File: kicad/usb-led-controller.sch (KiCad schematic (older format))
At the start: 2 parts

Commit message: Adding initial schematic
The PWM outputs are driven with the microcontroller PWM. The WS2812
outputs are driven from UARTS with DMA capability.
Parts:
- removed J?: Conn_02x05_Odd_Even, symbol Connector_Generic:Conn_02x05_Odd_Even
- added C1: 4u7, Capacitor_SMD:C_0805_2012Metric, symbol Device:C
- added C2, C4, C8: 1u, Capacitor_SMD:C_0402_1005Metric, symbol Device:C
- added C3: 10u, Capacitor_SMD:C_0805_2012Metric, symbol Device:C
- added C5, C6, C7: 0u1, Capacitor_SMD:C_0402_1005Metric, symbol Device:C
- added J1: SWD, usb-led-controller:JST-SH-4, symbol Connector_Generic:Conn_01x04
- added J2: PWR, usb-led-controller:M20-88904, symbol Connector_Generic:Conn_01x04
- added J3: USB, usb-led-controller:M20-88904, symbol Connector_Generic:Conn_01x04
- added J4: PWM_0, usb-led-controller:M20-88904, symbol Connector_Generic:Conn_01x04
- added J5: PWM_1, usb-led-controller:M20-88904, symbol Connector_Generic:Conn_01x04
- added J6: WS2812_0, usb-led-controller:M20-88903, symbol Connector_Generic:Conn_01x03
- added J7: WS2812_1, usb-led-controller:M20-88903, symbol Connector_Generic:Conn_01x03
- added Q1, Q2, Q3, Q4, Q5, Q6: NVS4409N, Package_TO_SOT_SMD:SOT-323_SC-70, symbol Device:Q_NMOS_GSD
- added R1, R3, R5: 0, Resistor_SMD:R_0402_1005Metric, symbol Device:R
- added R2: 1K, Resistor_SMD:R_0402_1005Metric, symbol Device:R
- added R4: SPR, Resistor_SMD:R_0402_1005Metric, symbol Device:R
- added R6, R7, R8, R9: 33, Resistor_SMD:R_0402_1005Metric, symbol Device:R
- added U1, U2: SN74LV1T04, Package_TO_SOT_SMD:SOT-353_SC-70-5, symbol usb-led-controller:SN74LV1T04
- added U4: MIC5501-XYM5, Package_TO_SOT_SMD:SOT-23-5, symbol usb-led-controller:MIC5501-XYM5
- added U5: USBLC6, Package_TO_SOT_SMD:SOT-666, symbol usb-led-controller:USBLC6
- gave numbers to parts that had none: 1
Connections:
- net labels added: +12V, +3.3V, BOOT0, GATE_0_B, GATE_0_G, GATE_0_R, GATE_1_B, GATE_1_G, GATE_1_R, NRST, PWM_0_B, PWM_0_G, PWM_0_R, PWM_1_B, PWM_1_G, PWM_1_R, SWCLK, SWDIO, USB_D+, USB_D-, USB_D_R+, USB_D_R-, USB_D_TVS+, USB_D_TVS-, WS2812_0_DATA, WS2812_0_DATA_IO, WS2812_0_DATA_R, WS2812_1_DATA, WS2812_1_DATA_IO, WS2812_1_DATA_R
- wire segments 6 -> 164
- no-connect marks 5 -> 16
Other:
- note added: "PA0: TIM2_CH1\nPA1: TIM2_CH2\nPA2: TIM2_CH3\nPA3: TIM2_CH4\nPA6: TIM22_CH1\nPA7: TIM22_CH2\nPA9: USART1_TX\nPA14: USART2_TX (yep...hopefully no bricking)"
- moved on the sheet: U3

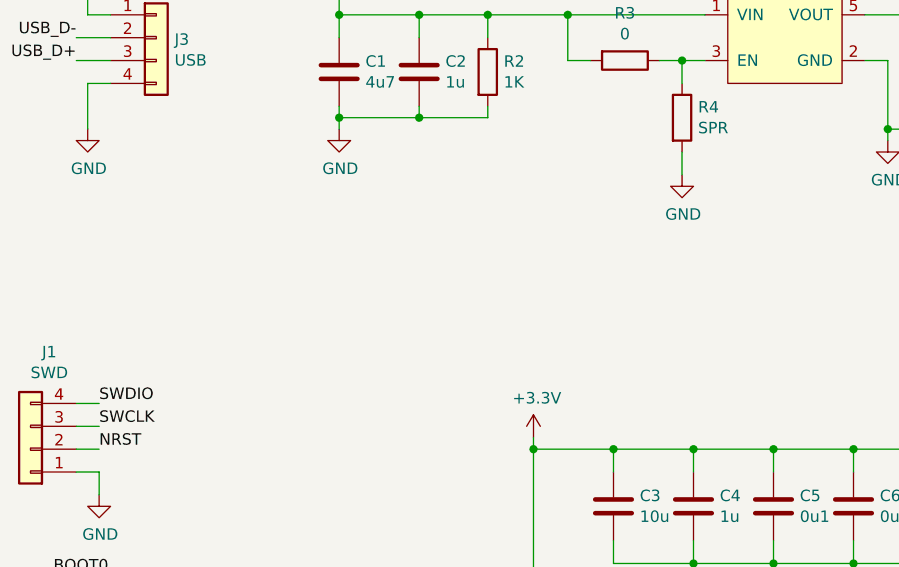
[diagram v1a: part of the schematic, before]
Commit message: Determined board form factor and placed connectors
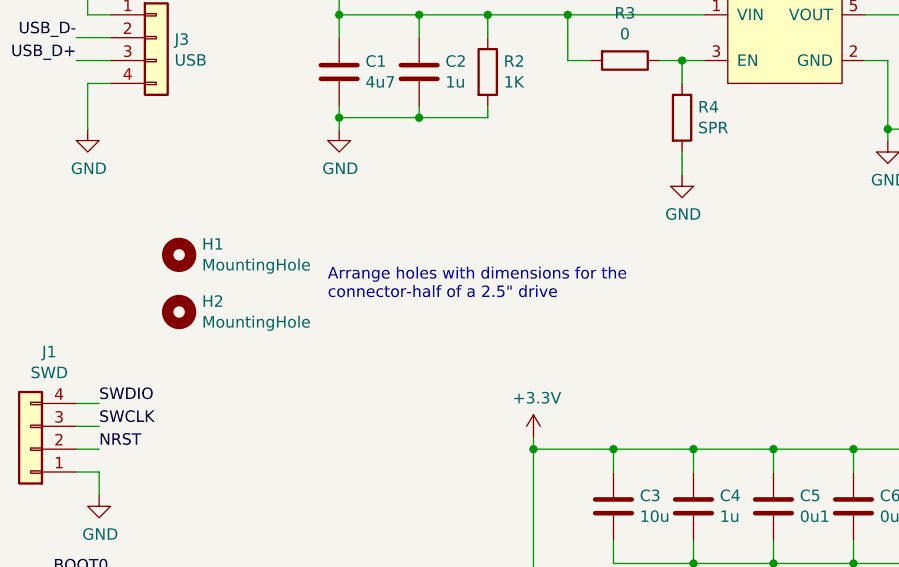
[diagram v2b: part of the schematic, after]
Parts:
- added H1, H2: MountingHole, MountingHole:MountingHole_3.2mm_M3, symbol Mechanical:MountingHole
- U5: Part Number (none) -> 497-5026-2-ND
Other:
- note added: "Arrange holes with dimensions for the\nconnector-half of a 2.5" drive"
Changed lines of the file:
@@
 F 2 "Package_TO_SOT_SMD:SOT-666" H 5300 4900 50  0001 C CNN
 F 3 "" H 5300 4900 50  0001 C CNN
+F 4 "497-5026-2-ND" H 5300 4900 50  0001 C CNN "Part Number"
 	1    5300 4900
 	1    0    0    -1
@@
 	1    0    0    -1
 $EndComp
+$Comp
+L Mechanical:MountingHole H1
+U 1 1 5FDF827D
+P 1450 2050
+F 0 "H1" H 1550 2096 50  0000 L CNN
+F 1 "MountingHole" H 1550 2005 50  0000 L CNN
+F 2 "MountingHole:MountingHole_3.2mm_M3" H 1450 2050 50  0001 C CNN
+F 3 "~" H 1450 2050 50  0001 C CNN
+	1    1450 2050
+	1    0    0    -1
+$EndComp
+$Comp
+L Mechanical:MountingHole H2
+U 1 1 5FDF8F49
+P 1450 2300
+F 0 "H2" H 1550 2346 50  0000 L CNN
+F 1 "MountingHole" H 1550 2255 50  0000 L CNN
+F 2 "MountingHole:MountingHole_3.2mm_M3" H 1450 2300 50  0001 C CNN
+F 3 "~" H 1450 2300 50  0001 C CNN
+	1    1450 2300
+	1    0    0    -1
+$EndComp
+Text Notes 2100 2250 0    50   ~ 0
+Arrange holes with dimensions for the\nconnector-half of a 2.5" drive
 $EndSCHEMATC

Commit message: Configuring 4-layer board stackup with netclasses
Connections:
- net REG_3V3_EN: now reaches R3.1, R4.1, U4.3 (EN)
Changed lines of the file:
@@
 Text Notes 2100 2250 0    50   ~ 0
 Arrange holes with dimensions for the\nconnector-half of a 2.5" drive
+Text Label 3650 1300 0    50   ~ 0
+REG_3V3_EN
 $EndSCHEMATC

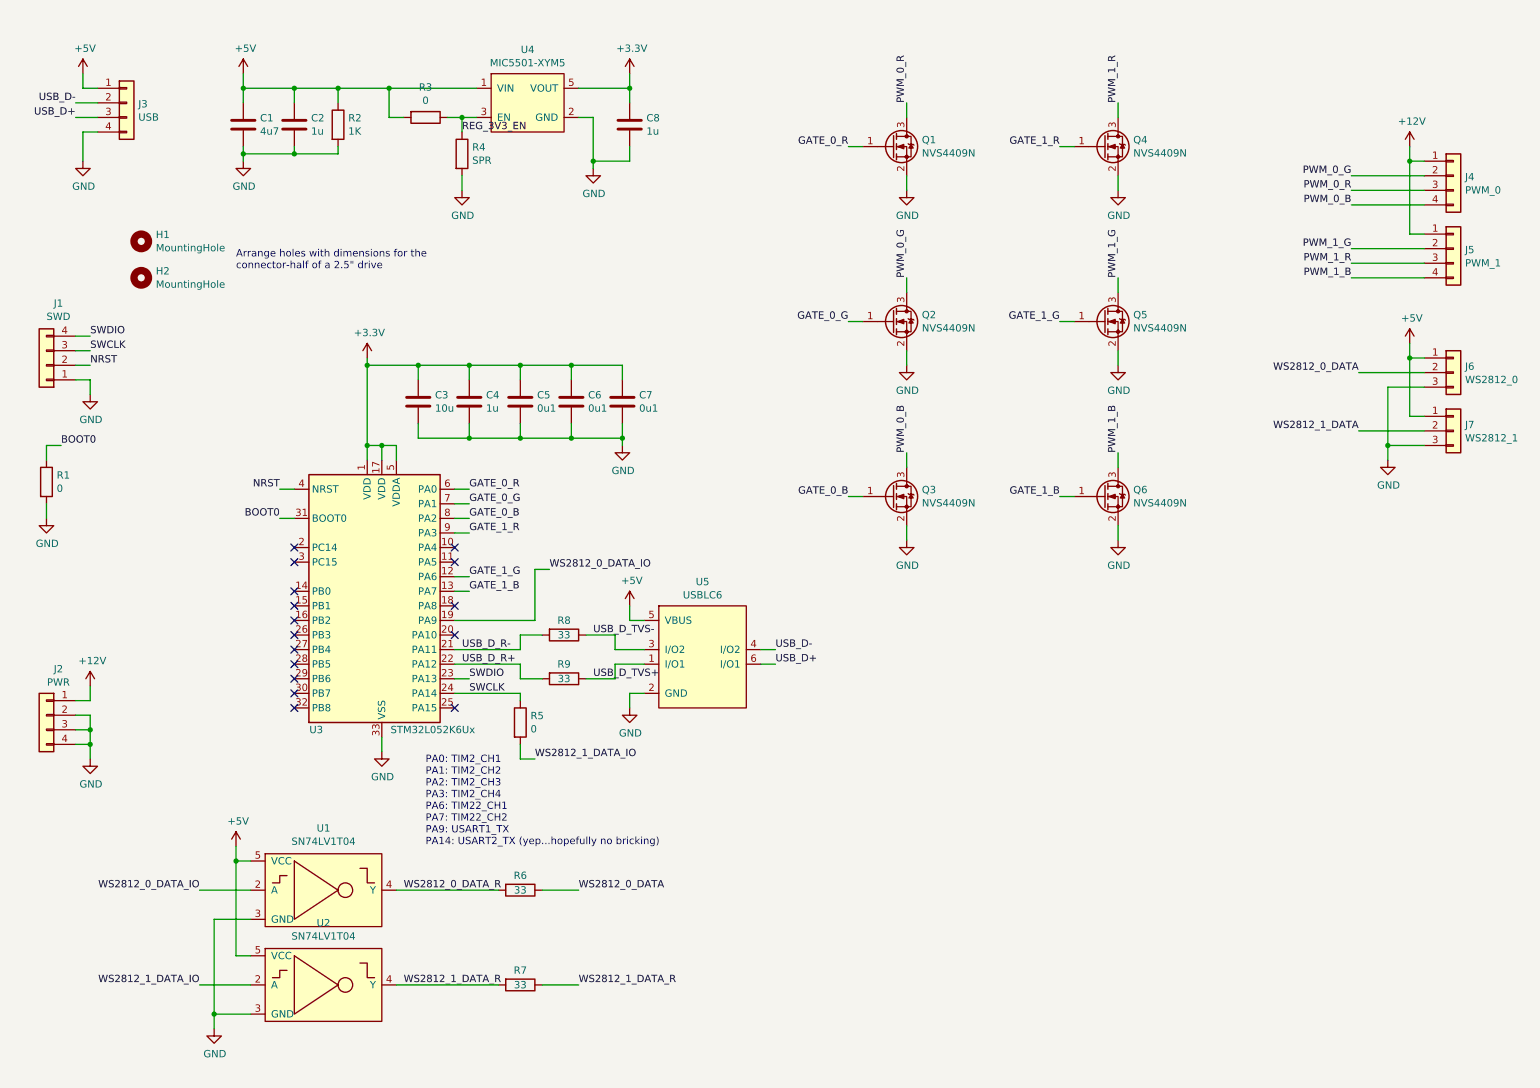
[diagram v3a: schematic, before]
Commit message: Changing microcontroller and redoing WS2812 control
The QFN package required VIPPO to be easily soldered. I could
probably have done it without plating-over, but it still requires the
heat gun and it is currently broken.

The family was downgraded to an ST32F042, which is a little clunkier
than the STM32L052 family. It also doesn't have very accessible UARTs
when USB is being used, so I swapped out the level shifters to tri-state
ones and used the remaining GPIOs as enables.
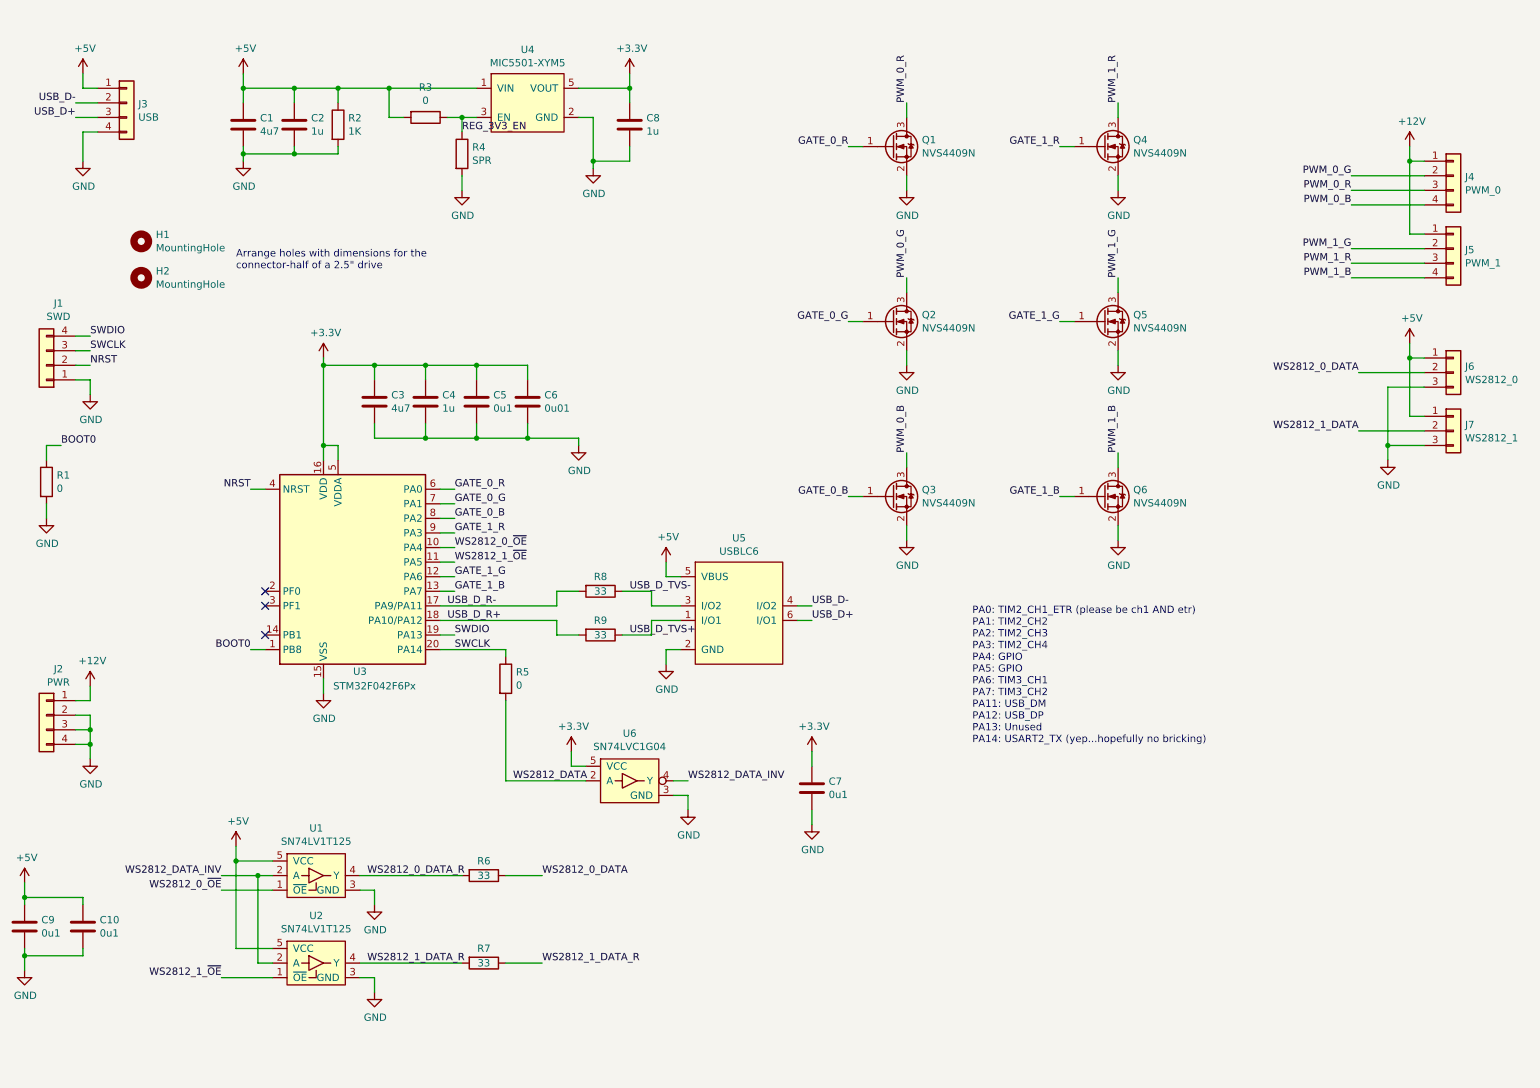
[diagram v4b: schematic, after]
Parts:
- removed U1, U2: SN74LV1T04, Package_TO_SOT_SMD:SOT-353_SC-70-5, symbol usb-led-controller:SN74LV1T04
- removed U3: STM32L052K6Ux, Package_DFN_QFN:QFN-32-1EP_5x5mm_P0.5mm_EP3.45x3.45mm, symbol MCU_ST_STM32L0:STM32L052K6Ux
- added C10, C9: 0u1, Capacitor_SMD:C_0402_1005Metric, symbol Device:C
- added U1, U2: SN74LV1T125, Package_TO_SOT_SMD:SOT-353_SC-70-5, symbol usb-led-controller:SN74LV1T125
- added U3: STM32F042F6Px, Package_SO:TSSOP-20_4.4x6.5mm_P0.65mm, symbol MCU_ST_STM32F0:STM32F042F6Px
- added U6: SN74LVC1G04, Package_TO_SOT_SMD:SOT-353_SC-70-5, symbol usb-led-controller:SN74LVC1G04
- C1: footprint Capacitor_SMD:C_0805_2012Metric -> Capacitor_SMD:C_0603_1608Metric; Part Number (none) -> 1276-1044-2-ND
- C2, C4, C8: footprint Capacitor_SMD:C_0402_1005Metric -> Capacitor_SMD:C_0603_1608Metric; Part Number (none) -> 1276-1102-2-ND
- C3: value 10u -> 4u7; footprint Capacitor_SMD:C_0805_2012Metric -> Capacitor_SMD:C_0603_1608Metric; Part Number (none) -> 1276-1044-2-ND
- C5, C7: Part Number (none) -> 1276-1043-2-ND
- C6: value 0u1 -> 0u01; Part Number (none) -> 587-5482-2-ND
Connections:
- net +3V3: now also U3.16 (VDD), U3.5 (VDDA), U6.5 (VCC)
- net +5V: now also C10.1, C9.1, U1.5 (VCC), U2.5 (VCC)
- net BOOT0: now also U3.1 (PB8)
- net GATE_0_B: now also U3.8 (PA2)
- net GATE_0_G: now also U3.7 (PA1)
- net GATE_0_R: now also U3.6 (PA0)
- net GATE_1_B: now also U3.13 (PA7)
- net GATE_1_G: now also U3.12 (PA6)
- net GATE_1_R: now also U3.9 (PA3)
- net GND: now also C10.2, C9.2, U1.3 (GND), U2.3 (GND), U3.15 (VSS), U6.3 (GND)
- net NRST: now also U3.4 (NRST)
- net SWCLK: now also U3.20 (PA14)
- net SWDIO: now also U3.19 (PA13)
- net USB_D_R+: now also U3.18 (PA10/PA12)
- net USB_D_R-: now also U3.17 (PA9/PA11)
- net WS2812_0_DATA_R: now also U1.4 (Y)
- net WS2812_1_DATA_R: now also U2.4 (Y)
- net WS2812_1_DATA_IO renamed WS2812_DATA
- net WS2812_DATA: now also U6.2 (A)
- new net WS2812_0_~OE: U1.1 (~OE), U3.10 (PA4)
- new net WS2812_1_~OE: U2.1 (~OE), U3.11 (PA5)
- new net WS2812_DATA_INV: U1.2 (A), U2.2 (A), U6.4 (Y)
- no-connect marks 16 -> 3
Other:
- note added: "PA0: TIM2_CH1_ETR (please be ch1 AND etr)\nPA1: TIM2_CH2\nPA2: TIM2_CH3\nPA3: TIM2_CH4\nPA4: GPIO\nPA5: GPIO\nPA6: TIM3_CH1\nPA7: TIM3_CH2\nPA11: USB_DM\nPA12: USB_DP\nPA13: Unused\nPA14: USART2_TX (yep...hopefully no bricking)"
- note removed: "PA0: TIM2_CH1\nPA1: TIM2_CH2\nPA2: TIM2_CH3\nPA3: TIM2_CH4\nPA6: TIM22_CH1\nPA7: TIM22_CH2\nPA9: USART1_TX\nPA14: USART2_TX (yep...hopefully no bricking)"
- moved on the sheet: C3, C4, C5, C6, C7, R5, R6, R7, R8, R9, U5

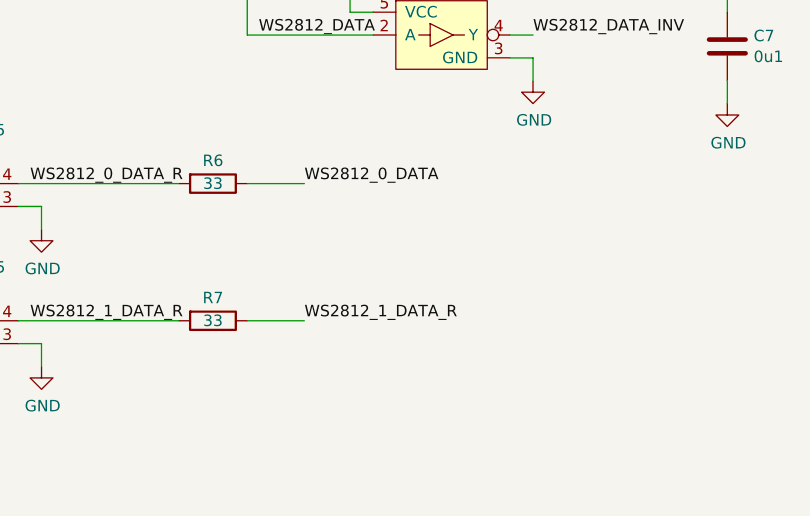
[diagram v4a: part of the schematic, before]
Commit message: Adding pulldowns on WS2812 outputs
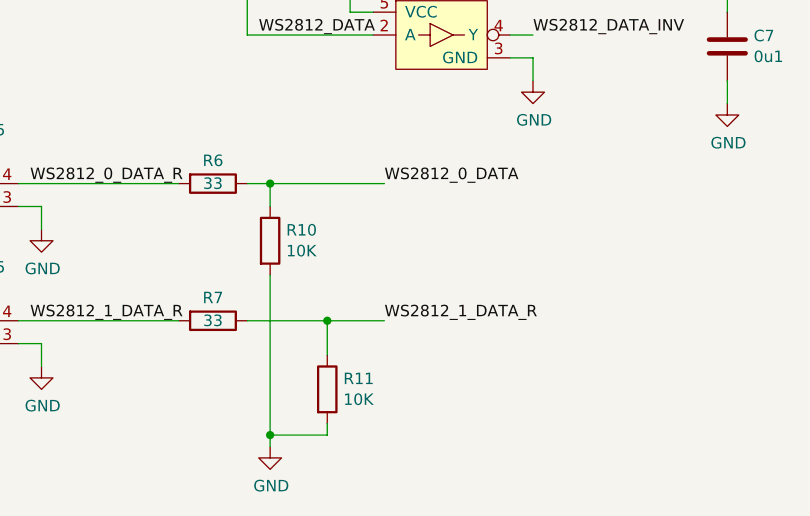
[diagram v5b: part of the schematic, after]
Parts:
- added R10, R11: 10K, Resistor_SMD:R_0402_1005Metric, symbol Device:R
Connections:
- net GND: now also R10.2, R11.2
- net WS2812_0_DATA: now also R10.1
- net WS2812_1_DATA_R: now also R11.1
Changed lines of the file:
@@
 Text Label 3000 7000 0    50   ~ 0
 WS2812_1_DATA_R
-Text Label 4200 6400 0    50   ~ 0
+Text Label 4550 6400 0    50   ~ 0
 WS2812_0_DATA
 Wire Wire Line
-	4200 6400 3950 6400
-Text Label 4200 7000 0    50   ~ 0
+	4550 6400 4050 6400
+Text Label 4550 7000 0    50   ~ 0
 WS2812_1_DATA_R
 Wire Wire Line
-	4200 7000 3950 7000
+	4550 7000 4300 7000
 Text Label 3600 3750 0    50   ~ 0
 GATE_0_R
@@
 Wire Wire Line
 	6050 6050 6050 5950
+$Comp
+L Device:R R11
+U 1 1 5FD87318
+P 4300 7300
+F 0 "R11" H 4370 7346 50  0000 L CNN
+F 1 "10K" H 4370 7255 50  0000 L CNN
+F 2 "Resistor_SMD:R_0402_1005Metric" V 4230 7300 50  0001 C CNN
+F 3 "~" H 4300 7300 50  0001 C CNN
+	1    4300 7300
+	1    0    0    -1
+$EndComp
+$Comp
+L Device:R R10
+U 1 1 5FD8889C
+P 4050 6650
+F 0 "R10" H 4120 6696 50  0000 L CNN
+F 1 "10K" H 4120 6605 50  0000 L CNN
+F 2 "Resistor_SMD:R_0402_1005Metric" V 3980 6650 50  0001 C CNN
+F 3 "~" H 4050 6650 50  0001 C CNN
+	1    4050 6650
+	1    0    0    -1
+$EndComp
+$Comp
+L power:GND #PWR01
+U 1 1 5FD8904A
+P 4050 7550
+F 0 "#PWR01" H 4050 7300 50  0001 C CNN
+F 1 "GND" H 4055 7377 50  0000 C CNN
+F 2 "" H 4050 7550 50  0001 C CNN
+F 3 "" H 4050 7550 50  0001 C CNN
+	1    4050 7550
+	1    0    0    -1
+$EndComp
+Wire Wire Line
+	4300 7150 4300 7000
+Connection ~ 4300 7000
+Wire Wire Line
+	4300 7000 3950 7000
+Wire Wire Line
+	4050 6500 4050 6400
+Connection ~ 4050 6400
+Wire Wire Line
+	4050 6400 3950 6400
+Wire Wire Line
+	4050 7550 4050 7500
+Wire Wire Line
+	4300 7450 4300 7500
+Wire Wire Line
+	4300 7500 4050 7500
+Connection ~ 4050 7500
+Wire Wire Line
+	4050 7500 4050 6800
 $EndSCHEMATC
